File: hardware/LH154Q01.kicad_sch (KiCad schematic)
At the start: 20 parts, among them IC2 MIC5501-3.0YM5-TR, J5 503548-1220, J8 FH35C-25S-0.3SHW_50_, U3 MIC3289

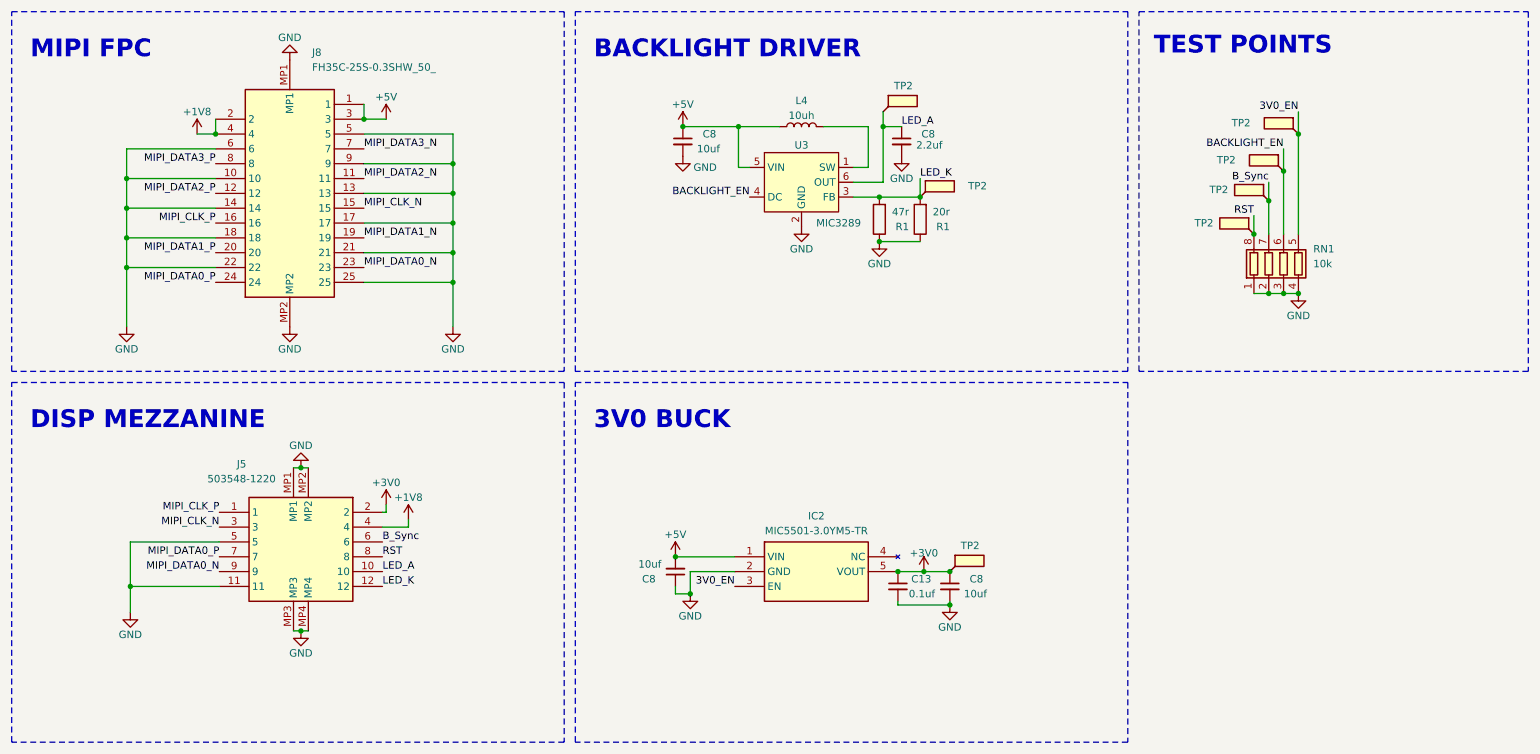
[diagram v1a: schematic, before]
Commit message: added via stitching and updated the bias generator layout
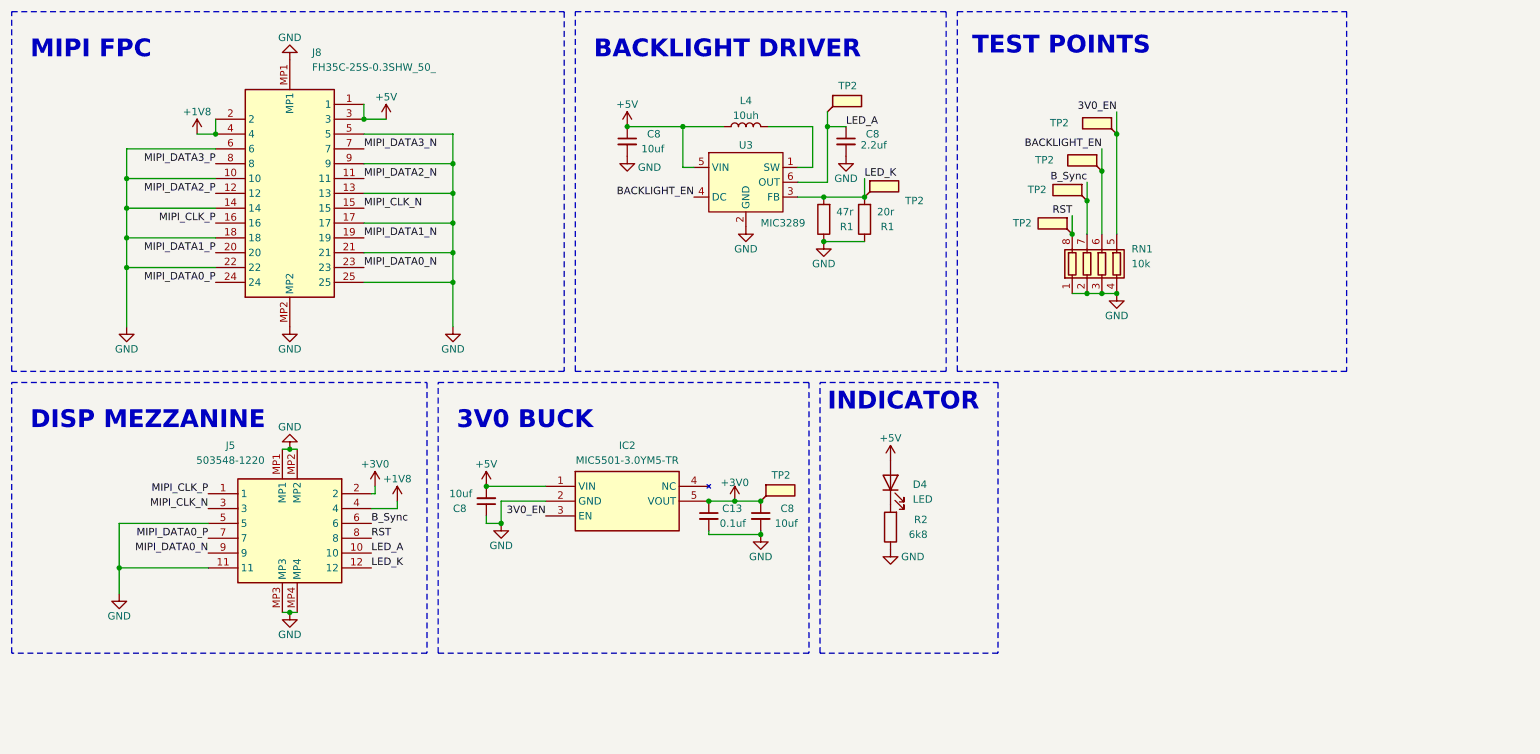
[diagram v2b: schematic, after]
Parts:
- added D4: LED, LED_SMD:LED_0805_2012Metric, symbol Device:LED
- added R2: 6k8, Resistor_SMD:R_0603_1608Metric, symbol Device:R
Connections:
- net +5V: now also D4.2 (A)
- net GND: now also R2.1
- new net: D4.1 (K), R2.2
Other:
- note added: "INDICATOR"
- moved on the sheet: C13, C8, IC2, J5, L4, R1, RN1, TP2, U3

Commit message: version 1.0
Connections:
- net +1V8: now also RN1.1 (R1.1)
- net GND: no longer RN1.1 (R1.1)
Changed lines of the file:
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@@
   (junction (at 197.485 45.72) (diameter 0) (color 0 0 0 0)
   )
-  (junction (at 197.485 61.595) (diameter 0) (color 0 0 0 0)
-  )
   (junction (at 128.27 33.02) (diameter 0) (color 0 0 0 0)
   )
@@
     (stroke (width 0) (type default))
   )
+  (wire (pts (xy 189.23 61.595) (xy 189.23 63.5))
+    (stroke (width 0) (type default))
+  )
   (wire (pts (xy 153.035 42.545) (xy 153.035 33.02))
     (stroke (width 0) (type default))
@@
     (stroke (width 0) (type default))
   )
-  (wire (pts (xy 194.945 61.595) (xy 197.485 61.595))
-    (stroke (width 0) (type default))
-  )
   (wire (pts (xy 200.025 36.83) (xy 200.025 40.64))
     (stroke (width 0) (type default))
@@
     (stroke (width 0) (type default))
   )
+  (wire (pts (xy 189.23 63.5) (xy 194.945 63.5))
+    (stroke (width 0) (type default))
+  )
   (wire (pts (xy 73.66 54.61) (xy 88.9 54.61))
     (stroke (width 0) (type default))
   )
   (wire (pts (xy 33.02 36.83) (xy 33.02 41.91))
+    (stroke (width 0) (type default))
+  )
+  (wire (pts (xy 194.945 63.5) (xy 194.945 61.595))
     (stroke (width 0) (type default))
   )
@@
         )
       )
+    )
+  )
+  (symbol (lib_id "power:+1V8") (at 189.23 61.595 0) (unit 1)
+    (in_bom yes) (on_board yes) (dnp no)
+    (property "Reference" "#PWR036" (at 189.23 65.405 0)
+      (effects (font (size 1.27 1.27)) hide)
+    )
+    (property "Value" "+1V8" (at 189.23 57.785 0)
+      (effects (font (size 1.27 1.27)))
+    )
+    (property "Footprint" "" (at 189.23 61.595 0)
+      (effects (font (size 1.27 1.27)) hide)
+    )
+    (property "Datasheet" "" (at 189.23 61.595 0)
+      (effects (font (size 1.27 1.27)) hide)
+    )
+    (pin "1")
+    (instances
+      (project "ssd2828_board"
+        (path "/e63e39d7-6ac0-4ffd-8aa3-1841a4541b55/eadf4466-e824-4ab1-a46a-9025d68137a1"
+          (reference "#PWR036") (unit 1)
+        )
+        (path "/e63e39d7-6ac0-4ffd-8aa3-1841a4541b55/d0befddb-c525-47aa-a36b-f999bfb6acb2"
+          (reference "#PWR0104") (unit 1)
+        )
+      )

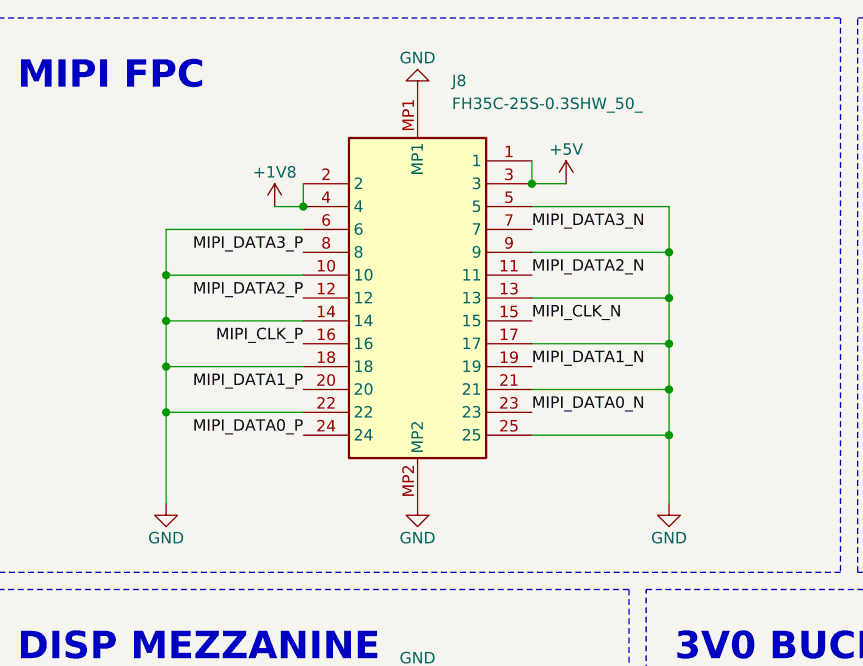
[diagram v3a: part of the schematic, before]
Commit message: fixed hirose FPC connector poinitng backwards on the 2 lcd boards+added stm32f401 boilerplate code
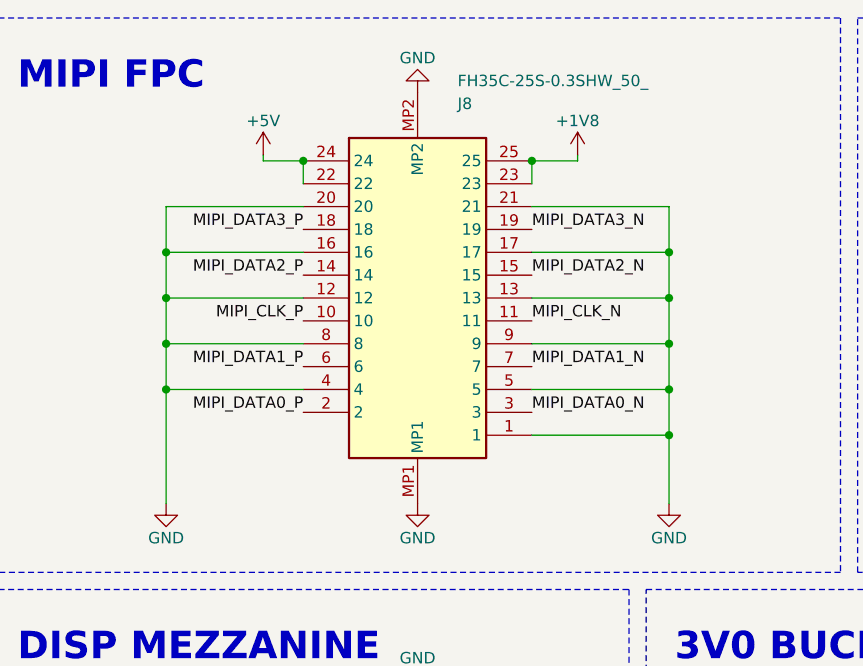
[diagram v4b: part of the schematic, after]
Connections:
- net +1V8: now also J8.23, J8.25; no longer J8.2, J8.4
- net +5V: now also J8.22, J8.24; no longer J8.1, J8.3
- net GND: now also J8.1, J8.12, J8.16, J8.20, J8.4, J8.8; no longer J8.10, J8.14, J8.18, J8.22, J8.25, J8.6
- net MIPI_CLK_N: now also J8.11; no longer J8.15
- net MIPI_CLK_P: now also J8.10; no longer J8.16
- net MIPI_DATA0_N: now also J8.3; no longer J8.23
- net MIPI_DATA0_P: now also J8.2; no longer J8.24
- net MIPI_DATA1_N: now also J8.7; no longer J8.19
- net MIPI_DATA1_P: now also J8.6; no longer J8.20
- net MIPI_DATA2_N: now also J8.15; no longer J8.11
- net MIPI_DATA2_P: now also J8.14; no longer J8.12
- net MIPI_DATA3_N: now also J8.19; no longer J8.7
- net MIPI_DATA3_P: now also J8.18; no longer J8.8
